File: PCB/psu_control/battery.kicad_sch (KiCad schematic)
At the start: 5 parts

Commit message: psu_control v4 is completed
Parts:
- D4, D5: renamed from D?; footprint (none) -> Connector_JST:JST_PH_B2B-PH-K_1x02_P2.00mm_Vertical
- J15: renamed from J?; footprint (none) -> Connector_JST:JST_PH_B5B-PH-K_1x05_P2.00mm_Vertical
- R37, R38: renamed from R?; footprint (none) -> Resistor_SMD:R_0805_2012Metric
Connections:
- net BATTERY_SMBUS_SCL: now also J15.3 (Pin_3); no longer J15.4 (Pin_4), R37.1
- net BATTERY_SMBUS_SDA: now also J15.2 (Pin_2); no longer J15.5 (Pin_5), R38.1
- net BATTERY_STATUS: now also J15.4 (Pin_4), R37.1; no longer J15.3 (Pin_3)
- net CHARGER_STATUS: now also J15.5 (Pin_5), R38.1; no longer J15.2 (Pin_2)
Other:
- note added: "J15: JST PH Connector"
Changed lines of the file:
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@@
 (kicad_sch (version 20211123) (generator eeschema)
   (paper "A4")
+  (junction (at 67.31 22.86) (diameter 0) (color 0 0 0 0)
+  )
   (junction (at 86.36 20.32) (diameter 0) (color 0 0 0 0)
-  )
-  (junction (at 60.96 22.86) (diameter 0) (color 0 0 0 0)
-  )
-  (wire (pts (xy 39.37 22.86) (xy 60.96 22.86))
-    (stroke (width 0) (type default) (color 0 0 0 0))
   )
   (wire (pts (xy 86.36 48.26) (xy 86.36 52.07))
     (stroke (width 0) (type default) (color 0 0 0 0))
   )
-  (wire (pts (xy 86.36 20.32) (xy 87.63 20.32))
+  (wire (pts (xy 67.31 22.86) (xy 68.58 22.86))
+    (stroke (width 0) (type default) (color 0 0 0 0))
+  )
+  (wire (pts (xy 86.36 20.32) (xy 86.36 31.75))
+    (stroke (width 0) (type default) (color 0 0 0 0))
+  )
+  (wire (pts (xy 39.37 22.86) (xy 67.31 22.86))
     (stroke (width 0) (type default) (color 0 0 0 0))
   )
@@
     (stroke (width 0) (type default) (color 0 0 0 0))
   )
-  (wire (pts (xy 60.96 22.86) (xy 62.23 22.86))
-    (stroke (width 0) (type default) (color 0 0 0 0))
-  )
   (wire (pts (xy 39.37 27.94) (xy 40.64 27.94))
     (stroke (width 0) (type default) (color 0 0 0 0))
   )
-  (wire (pts (xy 60.96 27.94) (xy 67.31 27.94))
+  (polyline (pts (xy 111.76 12.7) (xy 111.76 59.69))
     (stroke (width 0) (type default) (color 0 0 0 0))
   )
   (wire (pts (xy 39.37 25.4) (xy 40.64 25.4))
-    (stroke (width 0) (type default) (color 0 0 0 0))
-  )
-  (wire (pts (xy 86.36 20.32) (xy 86.36 31.75))
-    (stroke (width 0) (type default) (color 0 0 0 0))
-  )
-  (wire (pts (xy 67.31 27.94) (xy 67.31 31.75))
     (stroke (width 0) (type default) (color 0 0 0 0))
   )
@@
     (stroke (width 0) (type default) (color 0 0 0 0))
   )
+  (wire (pts (xy 86.36 20.32) (xy 87.63 20.32))
+    (stroke (width 0) (type default) (color 0 0 0 0))
+  )
+  (polyline (pts (xy 12.7 59.69) (xy 111.76 59.69))
+    (stroke (width 0) (type default) (color 0 0 0 0))
+  )
   (wire (pts (xy 40.64 30.48) (xy 40.64 31.75))
     (stroke (width 0) (type default) (color 0 0 0 0))
   )
-  (wire (pts (xy 60.96 22.86) (xy 60.96 27.94))
+  (wire (pts (xy 67.31 22.86) (xy 67.31 31.75))
     (stroke (width 0) (type default) (color 0 0 0 0))
   )
-  (text "Battery" (at 13.97 15.24 0)
-    (effects (font (size 1.27 1.27) bold) (justify left bottom))
+  (text "Battery" (at 13.97 16.51 0)
+    (effects (font (size 2.54 2.54)) (justify left bottom))
   )
-  (hierarchical_label "BATTERY_STATUS" (shape output) (at 40.64 25.4 0)
+  (text "J15: JST PH Connector" (at 87.63 15.24 0)
+    (effects (font (size 1.27 1.27)) (justify left bottom))
+  )
+  (hierarchical_label "BATTERY_STATUS" (shape output) (at 68.58 22.86 0)
     (effects (font (size 1.27 1.27)) (justify left))
   )
-  (hierarchical_label "BATTERY_SMBUS_SDA" (shape output) (at 87.63 20.32 0)
+  (hierarchical_label "BATTERY_SMBUS_SDA" (shape output) (at 40.64 27.94 0)
     (effects (font (size 1.27 1.27)) (justify left))
   )
-  (hierarchical_label "BATTERY_SMBUS_SCL" (shape output) (at 62.23 22.86 0)
+  (hierarchical_label "BATTERY_SMBUS_SCL" (shape output) (at 40.64 25.4 0)
     (effects (font (size 1.27 1.27)) (justify left))
   )
-  (hierarchical_label "CHARGER_STATUS" (shape output) (at 40.64 27.94 0)
+  (hierarchical_label "CHARGER_STATUS" (shape output) (at 87.63 20.32 0)
     (effects (font (size 1.27 1.27)) (justify left))
   )
   (symbol (lib_id "Device:R") (at 67.31 35.56 0) (unit 1)
     (in_bom yes) (on_board yes) (fields_autoplaced)
-    (property "Reference" "R?" (id 0) (at 69.85 34.2899 0)
+    (property "Reference" "R37" (id 0) (at 69.85 34.2899 0)
       (effects (font (size 1.27 1.27)) (justify left))
     )
@@
       (effects (font (size 1.27 1.27)) (justify left))
     )
-    (property "Footprint" "" (id 2) (at 65.532 35.56 90)
+    (property "Footprint" "Resistor_SMD:R_0805_2012Metric" (id 2) (at 65.532 35.56 90)
       (effects (font (size 1.27 1.27)) hide)
     )
@@
   (symbol (lib_id "Device:R") (at 86.36 35.56 0) (unit 1)
     (in_bom yes) (on_board yes) (fields_autoplaced)
-    (property "Reference" "R?" (id 0) (at 88.9 34.2899 0)
+    (property "Reference" "R38" (id 0) (at 88.9 34.2899 0)
       (effects (font (size 1.27 1.27)) (justify left))
     )
@@
       (effects (font (size 1.27 1.27)) (justify left))
     )
-    (property "Footprint" "" (id 2) (at 84.582 35.56 90)
+    (property "Footprint" "Resistor_SMD:R_0805_2012Metric" (id 2) (at 84.582 35.56 90)
       (effects (font (size 1.27 1.27)) hide)
     )
@@
   (symbol (lib_id "Device:LED") (at 67.31 44.45 90) (unit 1)
     (in_bom yes) (on_board yes) (fields_autoplaced)
-    (property "Reference" "D?" (id 0) (at 71.12 44.7674 90)
+    (property "Reference" "D4" (id 0) (at 71.12 44.7674 90)
       (effects (font (size 1.27 1.27)) (justify right))
     )
@@
       (effects (font (size 1.27 1.27)) (justify right))
     )
-    (property "Footprint" "" (id 2) (at 67.31 44.45 0)
+    (property "Footprint" "Connector_JST:JST_PH_B2B-PH-K_1x02_P2.00mm_Vertical" (id 2) (at 67.31 44.45 0)
       (effects (font (size 1.27 1.27)) hide)
     )
@@
   (symbol (lib_id "Device:LED") (at 86.36 44.45 90) (unit 1)
     (in_bom yes) (on_board yes) (fields_autoplaced)
-    (property "Reference" "D?" (id 0) (at 90.17 44.7674 90)
+    (property "Reference" "D5" (id 0) (at 90.17 44.7674 90)
       (effects (font (size 1.27 1.27)) (justify right))
     )
@@
       (effects (font (size 1.27 1.27)) (justify right))
     )
-    (property "Footprint" "" (id 2) (at 86.36 44.45 0)
+    (property "Footprint" "Connector_JST:JST_PH_B2B-PH-K_1x02_P2.00mm_Vertical" (id 2) (at 86.36 44.45 0)
       (effects (font (size 1.27 1.27)) hide)
     )
@@
   (symbol (lib_id "power:GND") (at 40.64 31.75 0) (unit 1)
     (in_bom yes) (on_board yes) (fields_autoplaced)
-    (property "Reference" "#PWR?" (id 0) (at 40.64 38.1 0)
+    (property "Reference" "#PWR0179" (id 0) (at 40.64 38.1 0)
       (effects (font (size 1.27 1.27)) hide)
     )
@@
   (symbol (lib_id "Connector:Conn_01x05_Male") (at 34.29 25.4 0) (mirror x) (unit 1)
     (in_bom yes) (on_board yes) (fields_autoplaced)
-    (property "Reference" "J?" (id 0) (at 33.02 24.1299 0)
+    (property "Reference" "J15" (id 0) (at 33.02 24.1299 0)
       (effects (font (size 1.27 1.27)) (justify right))
     )
@@
       (effects (font (size 1.27 1.27)) (justify right))
     )
-    (property "Footprint" "" (id 2) (at 34.29 25.4 0)
+    (property "Footprint" "Connector_JST:JST_PH_B5B-PH-K_1x05_P2.00mm_Vertical" (id 2) (at 34.29 25.4 0)
       (effects (font (size 1.27 1.27)) hide)
     )
@@
   (symbol (lib_id "power:GND") (at 67.31 52.07 0) (unit 1)
     (in_bom yes) (on_board yes) (fields_autoplaced)
-    (property "Reference" "#PWR?" (id 0) (at 67.31 58.42 0)
+    (property "Reference" "#PWR0177" (id 0) (at 67.31 58.42 0)
       (effects (font (size 1.27 1.27)) hide)
     )
@@
   (symbol (lib_id "power:GND") (at 86.36 52.07 0) (unit 1)
     (in_bom yes) (on_board yes) (fields_autoplaced)
-    (property "Reference" "#PWR?" (id 0) (at 86.36 58.42 0)
+    (property "Reference" "#PWR0178" (id 0) (at 86.36 58.42 0)
       (effects (font (size 1.27 1.27)) hide)
     )

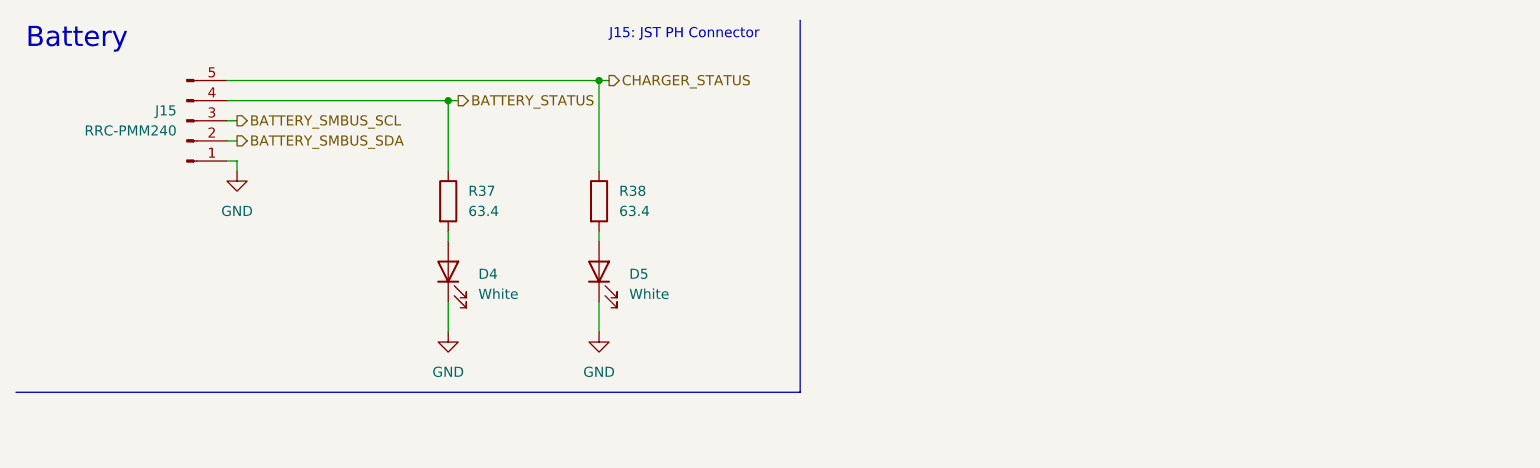
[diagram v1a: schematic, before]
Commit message: Add dynamixel_control PCB
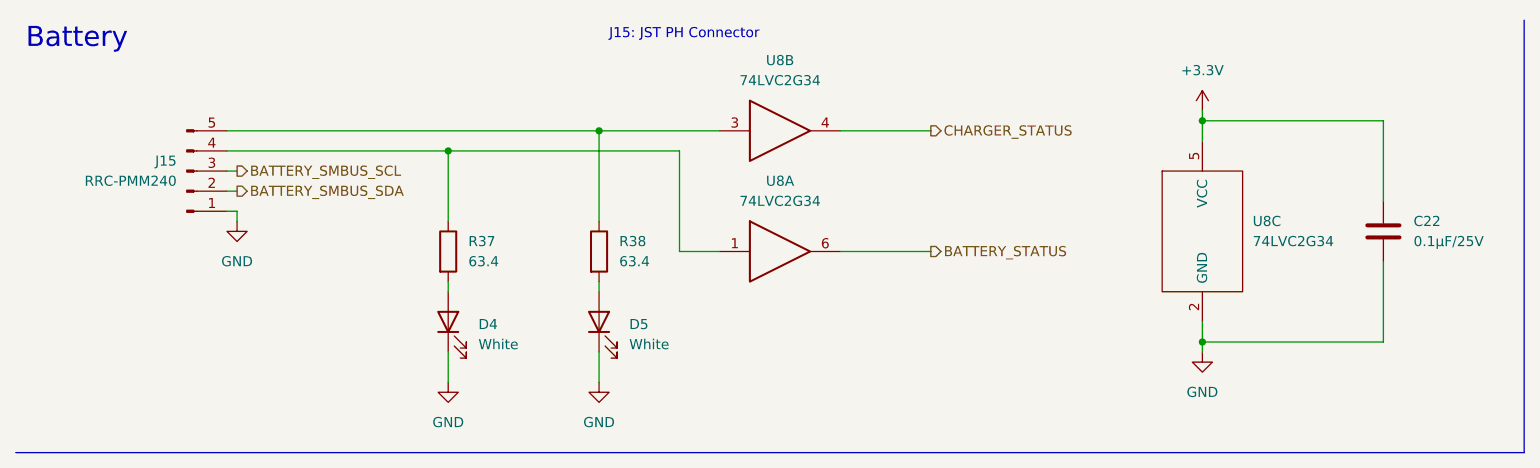
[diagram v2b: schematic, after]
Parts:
- added C22: 0.1µF/25V, Capacitor_SMD:C_0805_2012Metric, symbol Device:C
- added U8: 74LVC2G34, Package_SO:TSOP-6_1.65x3.05mm_P0.95mm, symbol t-top:74LVC2G34
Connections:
- net BATTERY_STATUS: now also U8.6; no longer J15.4 (Pin_4), R37.1
- net CHARGER_STATUS: now also U8.4; no longer J15.5 (Pin_5), R38.1
- net GND: now also C22.2, U8.2 (GND)
- new net: J15.4 (Pin_4), R37.1, U8.1
- new net: J15.5 (Pin_5), R38.1, U8.3
- new net +3.3V: C22.1, U8.5 (VCC)
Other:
- moved on the sheet: D4, D5, J15, R37, R38

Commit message: Fix issues. Add schematic files.
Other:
- note added: "U8 is useful to prevent apply voltage to the Teensy when it is unpowered."
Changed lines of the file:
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@@
     (effects (font (size 2.54 2.54)) (justify left bottom))
+  )
+  (text "U8 is useful to prevent apply voltage to the Teensy when it is unpowered."
+    (at 93.98 66.04 0)
+    (effects (font (size 1.27 1.27)) (justify left bottom))
   )
   (text "J15: JST PH Connector" (at 87.63 15.24 0)

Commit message: Fix PCBs.
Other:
- note added: "U8 is useful to prevent applying voltage to the Teensy when it is unpowered."
- note removed: "U8 is useful to prevent apply voltage to the Teensy when it is unpowered."
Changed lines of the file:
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@@
     (effects (font (size 2.54 2.54)) (justify left bottom))
   )
-  (text "U8 is useful to prevent apply voltage to the Teensy when it is unpowered."
+  (text "U8 is useful to prevent applying voltage to the Teensy when it is unpowered."
     (at 93.98 66.04 0)
     (effects (font (size 1.27 1.27)) (justify left bottom))
